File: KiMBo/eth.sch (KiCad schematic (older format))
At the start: 45 parts, among them U1 OSD3358, U11 LAN8710A, Y1 7A-25.000MAAJ-T

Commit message: Assocate more footprints
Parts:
- C27, C28, C29, C30, C31, C32, C34: footprint Capacitors_SMD:C_0402 -> Capacitors_SMD:C_0603
- C35, C36, C37, C38: footprint Capacitors_SMD:C_0402 -> (none)
- FB28: footprint (none) -> Resistors_SMD:R_0805
- R54, R57, R58, R59, R60, R61, R62, R63, R64, R65, R66, R67, R68, R69, R70, R71, R72, R73, R74, R75, R76, R77, R78, R79, R80, R81, R82: footprint Resistors_SMD:R_0402 -> Resistors_SMD:R_0603
- U1: footprint (none) -> KiMBo:BGA-400-1-27mm
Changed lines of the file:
@@
 F 0 "R54" H 5019 5446 50  0000 L CNN
 F 1 "10Ω" H 5019 5355 50  0000 L CNN
-F 2 "Resistors_SMD:R_0402" V 4880 5400 50  0001 C CNN
+F 2 "Resistors_SMD:R_0603" V 4880 5400 50  0001 C CNN
 F 3 "" H 4950 5400 50  0000 C CNN
 	1    4950 5400
@@
 F 0 "C27" H 5064 5846 50  0000 L CNN
 F 1 "30pF" H 5064 5755 50  0000 L CNN
-F 2 "Capacitors_SMD:C_0402" H 4988 5650 50  0001 C CNN
+F 2 "Capacitors_SMD:C_0603" H 4988 5650 50  0001 C CNN
 F 3 "" H 4950 5800 50  0000 C CNN
 	1    4950 5800
@@
 F 0 "C28" H 5565 5846 50  0000 L CNN
 F 1 "30pF" H 5565 5755 50  0000 L CNN
-F 2 "Capacitors_SMD:C_0402" H 5488 5650 50  0001 C CNN
+F 2 "Capacitors_SMD:C_0603" H 5488 5650 50  0001 C CNN
 F 3 "" H 5450 5800 50  0000 C CNN
 	1    5450 5800
@@
 F 0 "R67" V 5550 5050 50  0000 C CNN
 F 1 "0Ω" V 5650 5050 50  0000 C CNN
-F 2 "Resistors_SMD:R_0402" V 5580 5050 50  0001 C CNN
+F 2 "Resistors_SMD:R_0603" V 5580 5050 50  0001 C CNN
 F 3 "" H 5650 5050 50  0000 C CNN
 	1    5650 5050
@@
 F 0 "R57" V 5200 3100 50  0000 C CNN
 F 1 "100Ω" V 5250 3300 50  0000 C CNN
-F 2 "Resistors_SMD:R_0402" V 5180 3300 50  0001 C CNN
+F 2 "Resistors_SMD:R_0603" V 5180 3300 50  0001 C CNN
 F 3 "" H 5250 3300 50  0000 C CNN
 	1    5250 3300
@@
 F 0 "R58" V 5200 3200 50  0000 C CNN
 F 1 "100Ω" V 5250 3400 50  0000 C CNN
-F 2 "Resistors_SMD:R_0402" V 5180 3400 50  0001 C CNN
+F 2 "Resistors_SMD:R_0603" V 5180 3400 50  0001 C CNN
 F 3 "" H 5250 3400 50  0000 C CNN
 	1    5250 3400
@@
 F 0 "R59" V 5200 3300 50  0000 C CNN
 F 1 "100Ω" V 5250 3500 50  0000 C CNN
-F 2 "Resistors_SMD:R_0402" V 5180 3500 50  0001 C CNN
+F 2 "Resistors_SMD:R_0603" V 5180 3500 50  0001 C CNN
 F 3 "" H 5250 3500 50  0000 C CNN
 	1    5250 3500
@@
 F 0 "R60" V 5200 3400 50  0000 C CNN
 F 1 "100Ω" V 5250 3600 50  0000 C CNN
-F 2 "Resistors_SMD:R_0402" V 5180 3600 50  0001 C CNN
+F 2 "Resistors_SMD:R_0603" V 5180 3600 50  0001 C CNN
 F 3 "" H 5250 3600 50  0000 C CNN
 	1    5250 3600
@@
 F 0 "R61" V 5200 3500 50  0000 C CNN
 F 1 "100Ω" V 5250 3700 50  0000 C CNN
-F 2 "Resistors_SMD:R_0402" V 5180 3700 50  0001 C CNN
+F 2 "Resistors_SMD:R_0603" V 5180 3700 50  0001 C CNN
 F 3 "" H 5250 3700 50  0000 C CNN
 	1    5250 3700
@@
 F 0 "R62" V 5200 3600 50  0000 C CNN
 F 1 "100Ω" V 5250 3800 50  0000 C CNN
-F 2 "Resistors_SMD:R_0402" V 5180 3800 50  0001 C CNN
+F 2 "Resistors_SMD:R_0603" V 5180 3800 50  0001 C CNN
 F 3 "" H 5250 3800 50  0000 C CNN
 	1    5250 3800
@@
 F 0 "R63" V 5200 3700 50  0000 C CNN
 F 1 "100Ω" V 5250 3900 50  0000 C CNN
-F 2 "Resistors_SMD:R_0402" V 5180 3900 50  0001 C CNN
+F 2 "Resistors_SMD:R_0603" V 5180 3900 50  0001 C CNN
 F 3 "" H 5250 3900 50  0000 C CNN
 	1    5250 3900
@@
 F 0 "R64" V 5200 3850 50  0000 C CNN
 F 1 "100Ω" V 5250 4050 50  0000 C CNN
-F 2 "Resistors_SMD:R_0402" V 5180 4050 50  0001 C CNN
+F 2 "Resistors_SMD:R_0603" V 5180 4050 50  0001 C CNN
 F 3 "" H 5250 4050 50  0000 C CNN
 	1    5250 4050
@@
 F 0 "R65" V 5200 4450 50  0000 C CNN
 F 1 "100Ω" V 5250 4650 50  0000 C CNN
-F 2 "Resistors_SMD:R_0402" V 5180 4650 50  0001 C CNN
+F 2 "Resistors_SMD:R_0603" V 5180 4650 50  0001 C CNN
 F 3 "" H 5250 4650 50  0000 C CNN
 	1    5250 4650
@@
 F 0 "R66" V 5200 4550 50  0000 C CNN
 F 1 "100Ω" V 5250 4750 50  0000 C CNN
-F 2 "Resistors_SMD:R_0402" V 5180 4750 50  0001 C CNN
+F 2 "Resistors_SMD:R_0603" V 5180 4750 50  0001 C CNN
 F 3 "" H 5250 4750 50  0000 C CNN
 	1    5250 4750
@@
 F 0 "R70" H 8400 3050 50  0000 L CNN
 F 1 "49.9Ω" H 8350 2750 50  0000 L CNN
-F 2 "Resistors_SMD:R_0402" V 8280 2900 50  0001 C CNN
+F 2 "Resistors_SMD:R_0603" V 8280 2900 50  0001 C CNN
 F 3 "" H 8350 2900 50  0000 C CNN
 	1    8350 2900
@@
 F 0 "R73" H 8600 3050 50  0000 L CNN
 F 1 "49.9Ω" H 8550 2750 50  0000 L CNN
-F 2 "Resistors_SMD:R_0402" V 8480 2900 50  0001 C CNN
+F 2 "Resistors_SMD:R_0603" V 8480 2900 50  0001 C CNN
 F 3 "" H 8550 2900 50  0000 C CNN
 	1    8550 2900
@@
 F 0 "R75" H 8800 3050 50  0000 L CNN
 F 1 "49.9Ω" H 8750 2750 50  0000 L CNN
-F 2 "Resistors_SMD:R_0402" V 8680 2900 50  0001 C CNN
+F 2 "Resistors_SMD:R_0603" V 8680 2900 50  0001 C CNN
 F 3 "" H 8750 2900 50  0000 C CNN
 	1    8750 2900
@@
 F 0 "R77" H 9000 3050 50  0000 L CNN
 F 1 "49.9Ω" H 8950 2750 50  0000 L CNN
-F 2 "Resistors_SMD:R_0402" V 8880 2900 50  0001 C CNN
+F 2 "Resistors_SMD:R_0603" V 8880 2900 50  0001 C CNN
 F 3 "" H 8950 2900 50  0000 C CNN
 	1    8950 2900
@@
 F 0 "C35" H 8350 3750 50  0000 L CNN
 F 1 "DNP-15pF" H 8350 3550 50  0000 L CNN
-F 2 "Capacitors_SMD:C_0402" H 8388 3500 50  0001 C CNN
+F 2 "" H 8388 3500 50  0001 C CNN
 F 3 "" H 8350 3650 50  0000 C CNN
 	1    8350 3650
@@
 F 0 "C36" H 8550 3750 50  0000 L CNN
 F 1 "DNP-15pF" H 8550 3500 50  0000 L CNN
-F 2 "Capacitors_SMD:C_0402" H 8588 3500 50  0001 C CNN
+F 2 "" H 8588 3500 50  0001 C CNN
 F 3 "" H 8550 3650 50  0000 C CNN
 	1    8550 3650
@@
 F 0 "C37" H 8750 3750 50  0000 L CNN
 F 1 "DNP-15pF" H 8750 3550 50  0000 L CNN
-F 2 "Capacitors_SMD:C_0402" H 8788 3500 50  0001 C CNN
+F 2 "" H 8788 3500 50  0001 C CNN
 F 3 "" H 8750 3650 50  0000 C CNN
 	1    8750 3650
@@
 F 0 "C38" H 8950 3750 50  0000 L CNN
 F 1 "DNP-15pF" H 8950 3500 50  0000 L CNN
-F 2 "Capacitors_SMD:C_0402" H 8988 3500 50  0001 C CNN
+F 2 "" H 8988 3500 50  0001 C CNN
 F 3 "" H 8950 3650 50  0000 C CNN
 	1    8950 3650
@@
 F 0 "R71" H 8520 5446 50  0000 L CNN
 F 1 "12.1kΩ" H 8520 5355 50  0000 L CNN
-F 2 "Resistors_SMD:R_0402" V 8380 5400 50  0001 C CNN
+F 2 "Resistors_SMD:R_0603" V 8380 5400 50  0001 C CNN
 F 3 "" H 8450 5400 50  0000 C CNN
 	1    8450 5400
@@
 F 0 "R74" H 8770 5246 50  0000 L CNN
 F 1 "10kΩ" H 8770 5155 50  0000 L CNN
-F 2 "Resistors_SMD:R_0402" V 8630 5200 50  0001 C CNN
+F 2 "Resistors_SMD:R_0603" V 8630 5200 50  0001 C CNN
 F 3 "" H 8700 5200 50  0000 C CNN
 	1    8700 5200
@@
 F 0 "R69" H 6219 2946 50  0000 L CNN
 F 1 "1.5kΩ" H 6185 2830 50  0000 L CNN
-F 2 "Resistors_SMD:R_0402" V 6080 2900 50  0001 C CNN
+F 2 "Resistors_SMD:R_0603" V 6080 2900 50  0001 C CNN
 F 3 "" H 6150 2900 50  0000 C CNN
 	1    6150 2900
@@
 F 0 "FB28" V 6735 2450 50  0000 C CNN
 F 1 "LI0805H151R-10" V 6650 2550 50  0000 C CNN
-F 2 "" H 6550 2450 50  0001 C CNN
+F 2 "Resistors_SMD:R_0805" H 6550 2450 50  0001 C CNN
 F 3 "" H 6550 2450 50  0000 C CNN
 	1    6550 2450
@@
 F 0 "C29" H 6015 2696 50  0000 L CNN
 F 1 "100nF" H 6015 2605 50  0000 L CNN
-F 2 "Capacitors_SMD:C_0402" H 5938 2500 50  0001 C CNN
+F 2 "Capacitors_SMD:C_0603" H 5938 2500 50  0001 C CNN
 F 3 "" H 5900 2650 50  0000 C CNN
 	1    5900 2650
@@
 F 0 "C30" H 7500 1850 50  0000 L CNN
 F 1 "100nF" H 7500 1650 50  0000 L CNN
-F 2 "Capacitors_SMD:C_0402" H 7538 1600 50  0001 C CNN
+F 2 "Capacitors_SMD:C_0603" H 7538 1600 50  0001 C CNN
 F 3 "" H 7500 1750 50  0000 C CNN
 	1    7500 1750
@@
 F 0 "C32" H 7750 2550 50  0000 L CNN
 F 1 "470pF" H 7700 2350 50  0000 L CNN
-F 2 "Capacitors_SMD:C_0402" H 7738 2300 50  0001 C CNN
+F 2 "Capacitors_SMD:C_0603" H 7738 2300 50  0001 C CNN
 F 3 "" H 7700 2450 50  0000 C CNN
 	1    7700 2450
@@
 F 0 "C34" H 8015 2496 50  0000 L CNN
 F 1 "1μF" H 8015 2405 50  0000 L CNN
-F 2 "Capacitors_SMD:C_0402" H 7938 2300 50  0001 C CNN
+F 2 "Capacitors_SMD:C_0603" H 7938 2300 50  0001 C CNN
 F 3 "" H 7900 2450 50  0000 C CNN
 	1    7900 2450
@@
 F 0 "C31" H 7700 1850 50  0000 L CNN
 F 1 "100nF" H 7700 1650 50  0000 L CNN
-F 2 "Capacitors_SMD:C_0402" H 7738 1600 50  0001 C CNN
+F 2 "Capacitors_SMD:C_0603" H 7738 1600 50  0001 C CNN
 F 3 "" H 7700 1750 50  0000 C CNN
 	1    7700 1750
@@
 F 0 "R68" V 5750 4800 50  0000 C CNN
 F 1 "DNP-0Ω" V 5925 4800 50  0000 C CNN
-F 2 "Resistors_SMD:R_0402" V 5780 4800 50  0001 C CNN
+F 2 "Resistors_SMD:R_0603" V 5780 4800 50  0001 C CNN
 F 3 "" H 5850 4800 50  0000 C CNN
 	1    5850 4800
@@
 F 0 "R72" H 8600 1500 50  0000 L CNN
 F 1 "10kΩ" H 8550 1300 50  0000 L CNN
-F 2 "Resistors_SMD:R_0402" V 8480 1450 50  0001 C CNN
+F 2 "Resistors_SMD:R_0603" V 8480 1450 50  0001 C CNN
 F 3 "" H 8550 1450 50  0000 C CNN
 	1    8550 1450
@@
 F 0 "R76" H 8850 1500 50  0000 L CNN
 F 1 "10kΩ" H 8800 1300 50  0000 L CNN
-F 2 "Resistors_SMD:R_0402" V 8730 1450 50  0001 C CNN
+F 2 "Resistors_SMD:R_0603" V 8730 1450 50  0001 C CNN
 F 3 "" H 8800 1450 50  0000 C CNN
 	1    8800 1450
@@
 F 0 "R78" H 9100 1500 50  0000 L CNN
 F 1 "10kΩ" H 9050 1300 50  0000 L CNN
-F 2 "Resistors_SMD:R_0402" V 8980 1450 50  0001 C CNN
+F 2 "Resistors_SMD:R_0603" V 8980 1450 50  0001 C CNN
 F 3 "" H 9050 1450 50  0000 C CNN
 	1    9050 1450
@@
 F 0 "R79" H 9370 1496 50  0000 L CNN
 F 1 "10kΩ" H 9370 1405 50  0000 L CNN
-F 2 "Resistors_SMD:R_0402" V 9230 1450 50  0001 C CNN
+F 2 "Resistors_SMD:R_0603" V 9230 1450 50  0001 C CNN
 F 3 "" H 9300 1450 50  0000 C CNN
 	1    9300 1450
@@
 F 0 "R80" H 10100 1200 50  0000 L CNN
 F 1 "1.5kΩ" H 10050 1000 50  0000 L CNN
-F 2 "Resistors_SMD:R_0402" V 9980 1150 50  0001 C CNN
+F 2 "Resistors_SMD:R_0603" V 9980 1150 50  0001 C CNN
 F 3 "" H 10050 1150 50  0000 C CNN
 	1    10050 1150
@@
 F 0 "R81" H 10350 1200 50  0000 L CNN
 F 1 "1.5kΩ" H 10300 1000 50  0000 L CNN
-F 2 "Resistors_SMD:R_0402" V 10230 1150 50  0001 C CNN
+F 2 "Resistors_SMD:R_0603" V 10230 1150 50  0001 C CNN
 F 3 "" H 10300 1150 50  0000 C CNN
 	1    10300 1150
@@
 F 0 "R82" H 10620 1196 50  0000 L CNN
 F 1 "1.5kΩ" H 10620 1105 50  0000 L CNN
-F 2 "Resistors_SMD:R_0402" V 10480 1150 50  0001 C CNN
+F 2 "Resistors_SMD:R_0603" V 10480 1150 50  0001 C CNN
 F 3 "" H 10550 1150 50  0000 C CNN
 	1    10550 1150
@@
 F 0 "U1" H 2550 1340 60  0000 C CNN
 F 1 "OSD3358" H 2550 1234 60  0000 C CNN
-F 2 "" H 1650 1050 60  0001 C CNN
+F 2 "KiMBo:BGA-400-1-27mm" H 1650 1050 60  0001 C CNN
 F 3 "" H 1650 1050 60  0001 C CNN
 	3    1650 1050

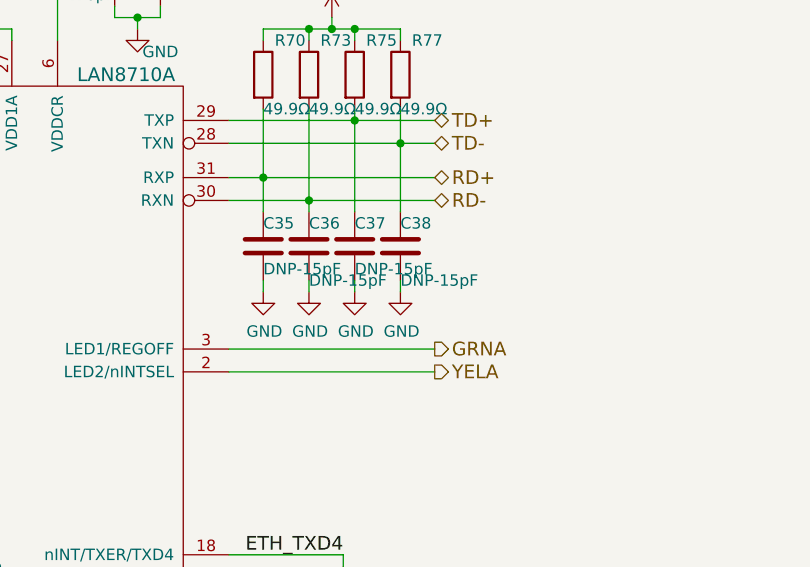
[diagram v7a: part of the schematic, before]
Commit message: More footprint association
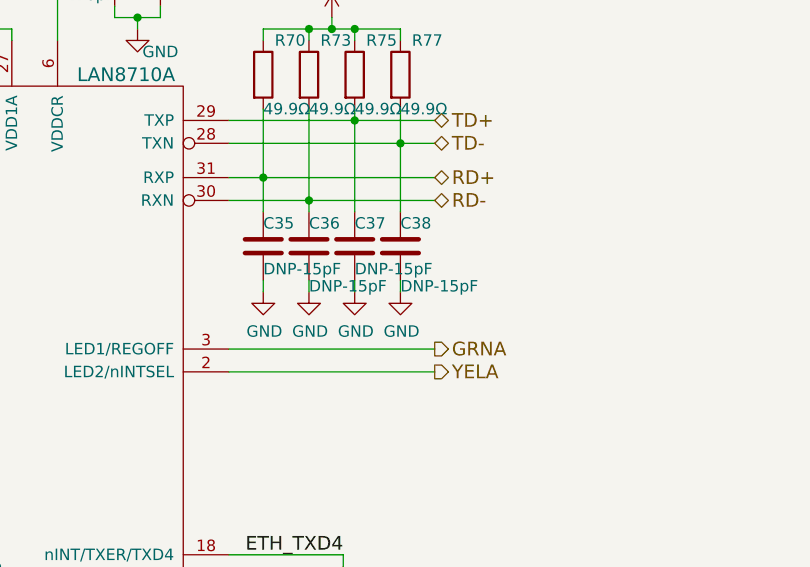
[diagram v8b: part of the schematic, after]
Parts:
- R68: footprint Resistors_SMD:R_0603 -> (none)
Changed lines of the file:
@@
 $EndComp
 $Comp
-L GND #PWR0120
+L GND #PWR0121
 U 1 1 589D3921
 P 4950 6000
-F 0 "#PWR0120" H 4950 5750 50  0001 C CNN
+F 0 "#PWR0121" H 4950 5750 50  0001 C CNN
 F 1 "GND" H 4955 5827 50  0000 C CNN
 F 2 "" H 4950 6000 50  0000 C CNN
@@
 $EndComp
 $Comp
-L GND #PWR0121
+L GND #PWR0122
 U 1 1 589D3945
 P 5450 6000
-F 0 "#PWR0121" H 5450 5750 50  0001 C CNN
+F 0 "#PWR0122" H 5450 5750 50  0001 C CNN
 F 1 "GND" H 5455 5827 50  0000 C CNN
 F 2 "" H 5450 6000 50  0000 C CNN
@@
 P 8550 3650
 F 0 "C36" H 8550 3750 50  0000 L CNN
-F 1 "DNP-15pF" H 8550 3500 50  0000 L CNN
+F 1 "DNP-15pF" H 8550 3475 50  0000 L CNN
 F 2 "" H 8588 3500 50  0001 C CNN
 F 3 "" H 8550 3650 50  0000 C CNN
@@
 P 8950 3650
 F 0 "C38" H 8950 3750 50  0000 L CNN
-F 1 "DNP-15pF" H 8950 3500 50  0000 L CNN
+F 1 "DNP-15pF" H 8950 3475 50  0000 L CNN
 F 2 "" H 8988 3500 50  0001 C CNN
 F 3 "" H 8950 3650 50  0000 C CNN
@@
 $EndComp
 $Comp
-L GND #PWR0122
+L GND #PWR0123
 U 1 1 589EF9C7
 P 8350 3850
-F 0 "#PWR0122" H 8350 3600 50  0001 C CNN
+F 0 "#PWR0123" H 8350 3600 50  0001 C CNN
 F 1 "GND" H 8355 3677 50  0000 C CNN
 F 2 "" H 8350 3850 50  0000 C CNN
@@
 $EndComp
 $Comp
-L GND #PWR0123
+L GND #PWR0124
 U 1 1 589EFA2D
 P 8550 3850
-F 0 "#PWR0123" H 8550 3600 50  0001 C CNN
+F 0 "#PWR0124" H 8550 3600 50  0001 C CNN
 F 1 "GND" H 8555 3677 50  0000 C CNN
 F 2 "" H 8550 3850 50  0000 C CNN
@@
 $EndComp
 $Comp
-L GND #PWR0124
+L GND #PWR0125
 U 1 1 589EFA8C
 P 8750 3850
-F 0 "#PWR0124" H 8750 3600 50  0001 C CNN
+F 0 "#PWR0125" H 8750 3600 50  0001 C CNN
 F 1 "GND" H 8755 3677 50  0000 C CNN
 F 2 "" H 8750 3850 50  0000 C CNN
@@
 $EndComp
 $Comp
-L GND #PWR0125
+L GND #PWR0126
 U 1 1 589EFAEB
 P 8950 3850
-F 0 "#PWR0125" H 8950 3600 50  0001 C CNN
+F 0 "#PWR0126" H 8950 3600 50  0001 C CNN
 F 1 "GND" H 8955 3677 50  0000 C CNN
 F 2 "" H 8950 3850 50  0000 C CNN
@@
 $EndComp
 $Comp
-L GND #PWR0126
+L GND #PWR0127
 U 1 1 589F5496
 P 7200 5600
-F 0 "#PWR0126" H 7200 5350 50  0001 C CNN
+F 0 "#PWR0127" H 7200 5350 50  0001 C CNN
 F 1 "GND" H 7205 5427 50  0000 C CNN
 F 2 "" H 7200 5600 50  0000 C CNN
@@
 $EndComp
 $Comp
-L GND #PWR0127
+L GND #PWR0128
 U 1 1 589F6033
 P 8450 5600
-F 0 "#PWR0127" H 8450 5350 50  0001 C CNN
+F 0 "#PWR0128" H 8450 5350 50  0001 C CNN
 F 1 "GND" H 8455 5427 50  0000 C CNN
 F 2 "" H 8450 5600 50  0000 C CNN
@@
 $EndComp
 $Comp
-L GND #PWR0128
+L GND #PWR0129
 U 1 1 589F60CA
 P 8700 5600
-F 0 "#PWR0128" H 8700 5350 50  0001 C CNN
+F 0 "#PWR0129" H 8700 5350 50  0001 C CNN
 F 1 "GND" H 8705 5427 50  0000 C CNN
 F 2 "" H 8700 5600 50  0000 C CNN
@@
 $EndComp
 $Comp
-L GND #PWR0129
+L GND #PWR0130
 U 1 1 589FBD44
 P 5900 2850
-F 0 "#PWR0129" H 5900 2600 50  0001 C CNN
+F 0 "#PWR0130" H 5900 2600 50  0001 C CNN
 F 1 "GND" H 5905 2677 50  0000 C CNN
 F 2 "" H 5900 2850 50  0000 C CNN
@@
 $EndComp
 $Comp
-L GND #PWR0130
+L GND #PWR0131
 U 1 1 589FC878
 P 7500 1950
-F 0 "#PWR0130" H 7500 1700 50  0001 C CNN
+F 0 "#PWR0131" H 7500 1700 50  0001 C CNN
 F 1 "GND" H 7505 1777 50  0000 C CNN
 F 2 "" H 7500 1950 50  0000 C CNN
@@
 $EndComp
 $Comp
-L GND #PWR0131
+L GND #PWR0132
 U 1 1 589FCD92
 P 7800 2700
-F 0 "#PWR0131" H 7800 2450 50  0001 C CNN
+F 0 "#PWR0132" H 7800 2450 50  0001 C CNN
 F 1 "GND" H 7900 2600 50  0000 C CNN
 F 2 "" H 7800 2700 50  0000 C CNN
@@
 $EndComp
 $Comp
-L GND #PWR0132
+L GND #PWR0133
 U 1 1 589FE46D
 P 7700 1950
-F 0 "#PWR0132" H 7700 1700 50  0001 C CNN
+F 0 "#PWR0133" H 7700 1700 50  0001 C CNN
 F 1 "GND" H 7705 1777 50  0000 C CNN
 F 2 "" H 7700 1950 50  0000 C CNN
@@
 $EndComp
 $Comp
-L GND #PWR0133
+L GND #PWR0134
 U 1 1 589FE4F9
 P 7900 1950
-F 0 "#PWR0133" H 7900 1700 50  0001 C CNN
+F 0 "#PWR0134" H 7900 1700 50  0001 C CNN
 F 1 "GND" H 7905 1777 50  0000 C CNN
 F 2 "" H 7900 1950 50  0000 C CNN
@@
 PHY_VDDCR
 $Comp
-L VDD_PHYA #PWR0134
+L VDD_PHYA #PWR0135
 U 1 1 58A03526
 P 7150 1500
-F 0 "#PWR0134" H 7150 1350 50  0001 C CNN
+F 0 "#PWR0135" H 7150 1350 50  0001 C CNN
 F 1 "VDD_PHYA" H 7165 1673 50  0000 C CNN
 F 2 "" H 7150 1500 50  0000 C CNN
@@
 $EndComp
 $Comp
-L VDD_PHYA #PWR0135
+L VDD_PHYA #PWR0136
 U 1 1 58A03EB3
 P 8650 2650
-F 0 "#PWR0135" H 8650 2500 50  0001 C CNN
+F 0 "#PWR0136" H 8650 2500 50  0001 C CNN
 F 1 "VDD_PHYA" H 8665 2823 50  0000 C CNN
 F 2 "" H 8650 2650 50  0000 C CNN
@@
 F 0 "R68" V 5750 4800 50  0000 C CNN
 F 1 "DNP-0Ω" V 5925 4800 50  0000 C CNN
-F 2 "Resistors_SMD:R_0603" V 5780 4800 50  0001 C CNN
+F 2 "" V 5780 4800 50  0001 C CNN
 F 3 "" H 5850 4800 50  0000 C CNN
 	1    5850 4800
@@
 RXER/PHYAD0
 $Comp
-L GND #PWR0136
+L GND #PWR0137
 U 1 1 58A0B062
 P 8550 1700
-F 0 "#PWR0136" H 8550 1450 50  0001 C CNN
+F 0 "#PWR0137" H 8550 1450 50  0001 C CNN
 F 1 "GND" H 8555 1527 50  0000 C CNN
 F 2 "" H 8550 1700 50  0000 C CNN
@@
 MMC0_CLK
 $Comp
-L VDD_3V3B #PWR0137
+L VDD_3V3B #PWR0138
 U 1 1 5A083952
 P 5900 2400
-F 0 "#PWR0137" H 5900 2250 50  0001 C CNN
+F 0 "#PWR0138" H 5900 2250 50  0001 C CNN
 F 1 "VDD_3V3B" H 5915 2573 50  0000 C CNN
 F 2 "" H 5900 2400 50  0000 C CNN
@@
 $EndComp
 $Comp
-L VDD_3V3B #PWR0138
+L VDD_3V3B #PWR0139
 U 1 1 5A08528B
 P 10300 900
-F 0 "#PWR0138" H 10300 750 50  0001 C CNN
+F 0 "#PWR0139" H 10300 750 50  0001 C CNN
 F 1 "VDD_3V3B" H 10315 1073 50  0000 C CNN
 F 2 "" H 10300 900 50  0000 C CNN
@@
 Connection ~ 6150 2700
 $Comp
-L PWR_FLAG #FLG0139
+L PWR_FLAG #FLG0140
 U 1 1 5A0AC399
 P 6850 2400
-F 0 "#FLG0139" H 6850 2495 50  0001 C CNN
+F 0 "#FLG0140" H 6850 2495 50  0001 C CNN
 F 1 "PWR_FLAG" H 6850 2624 50  0000 C CNN
 F 2 "" H 6850 2400 50  0000 C CNN
